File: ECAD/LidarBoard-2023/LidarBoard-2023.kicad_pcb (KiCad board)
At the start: 2 copper layers, 68.8 x 76.2 mm, 17 parts, among them J1 Serial_Strategy, J2 Serial_Lidar, J3 Conn_01x03, J4 Oled, U1 Teensy3.2, U2 AMS1117-3.3

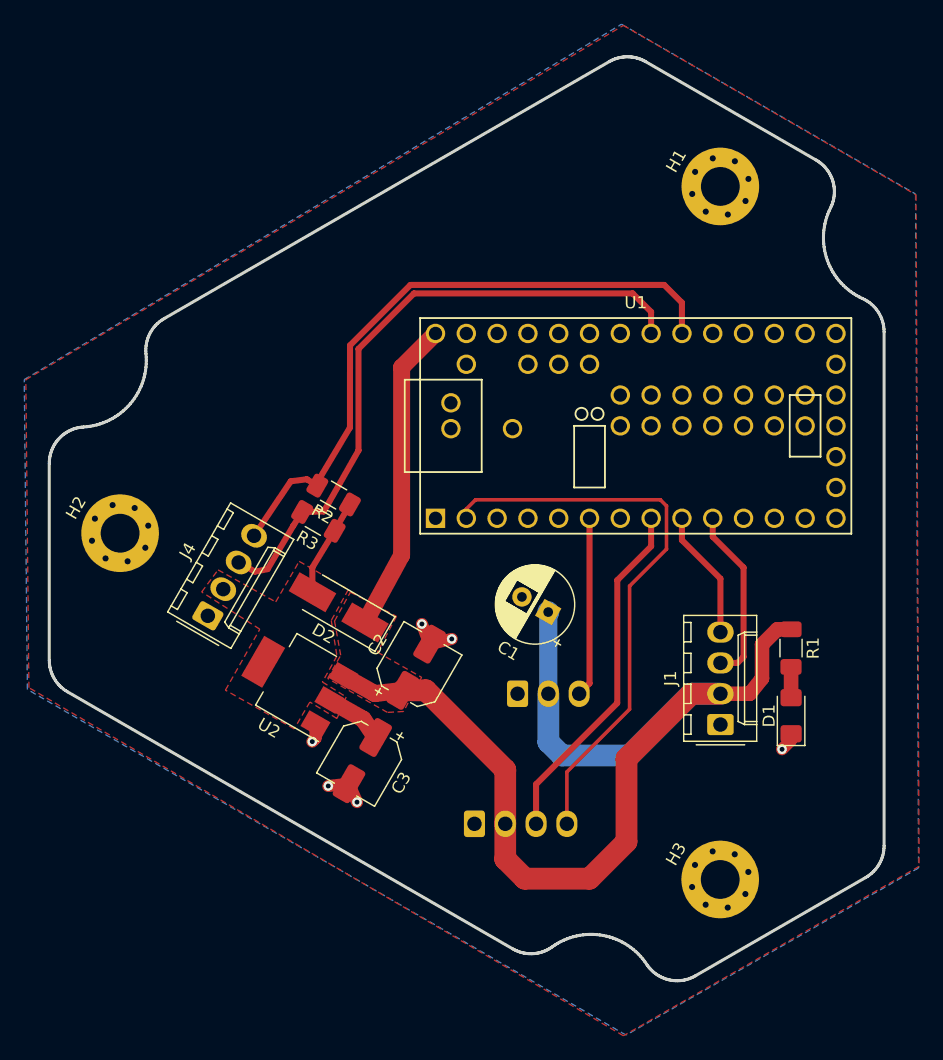
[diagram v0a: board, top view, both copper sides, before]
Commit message: Capacitor & silkscreen
Change output capacitor type to tantalum 1206 - 22uF
Update Silkscreen before production
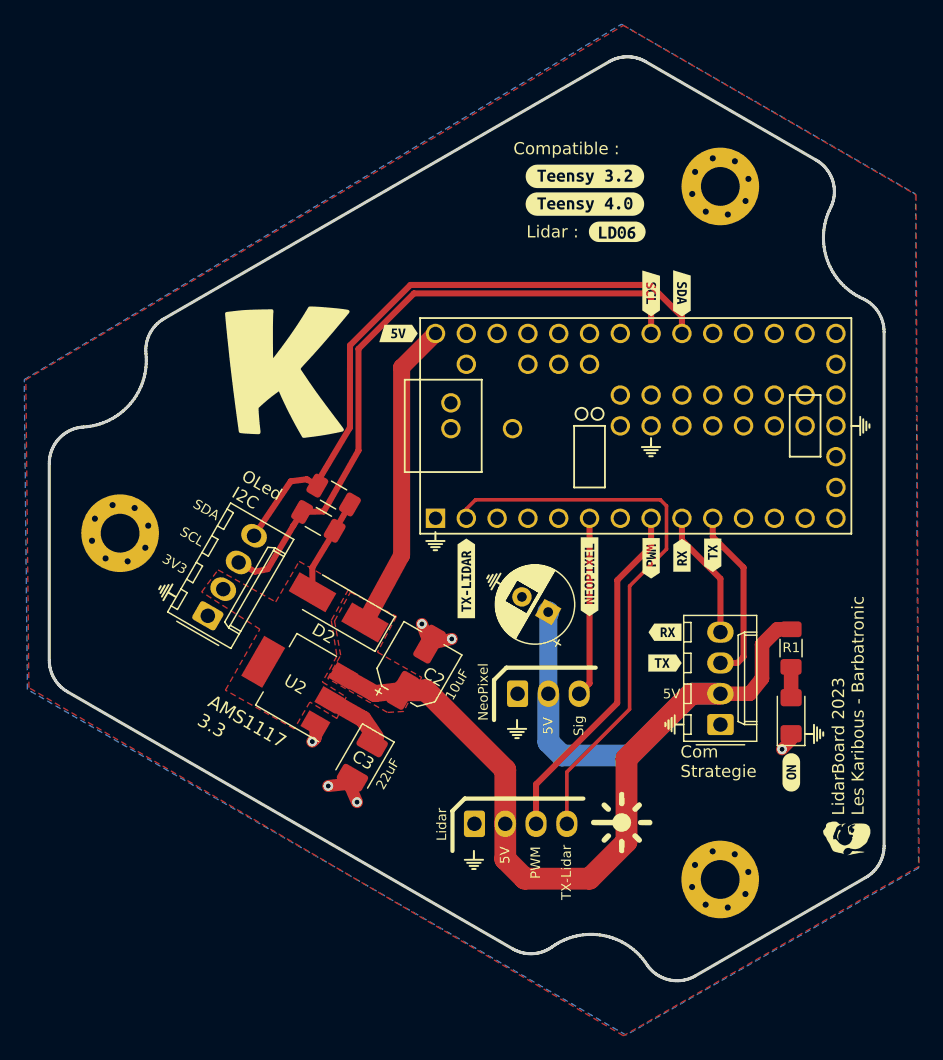
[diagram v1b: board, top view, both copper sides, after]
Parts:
- added G***: LOGO, LOGO, F.Cu at (157.5, 80.5)
- added G***: LOGO, LOGO, F.Cu at (174.8, 78.7)
- added G***: LOGO, LOGO, F.Cu at (170.9, 104.1)
- added G***: LOGO, LOGO, B.Cu at (142.9, 115.2)
- added G***: LOGO, LOGO, B.Cu at (146.4, 104.5)
- added G***: LOGO, LOGO, B.Cu at (159.3, 113.9)
- added G***: LOGO, LOGO, F.Cu at (117.6, 92.5)
- added G***: LOGO, LOGO, F.Cu at (146.4, 103.8)
- added G***: LOGO, LOGO, F.Cu at (159.3, 109.0)
- added G***: LOGO, LOGO, F.Cu at (139.7, 88.3)
- added G***: LOGO, LOGO, F.Cu at (142.9, 114.6)
- added G***: LOGO, LOGO, F.Cu at (144.7, 91.6)
- added G***: LOGO, LOGO, F.Cu at (159.4, 103.4)
- added G***: LOGO, LOGO, F.Cu at (173.6, 112.8)
- added kibuzzard-62EFEF5E: G***, kibuzzard-62EFEF5E, F.Cu at (152.0, 58.2)
- added kibuzzard-62EFEF6E: G***, kibuzzard-62EFEF6E, F.Cu at (152.0, 60.5)
- added kibuzzard-62EFEFDE: G***, kibuzzard-62EFEFDE, F.Cu at (154.7, 62.7)
- added kibuzzard-62EFF3FC: G***, kibuzzard-62EFF3FC, F.Cu at (160.0, 67.8)
- added kibuzzard-62EFF40D: G***, kibuzzard-62EFF40D, F.Cu at (157.5, 67.8)
- added kibuzzard-62EFF433: G***, kibuzzard-62EFF433, F.Cu at (136.7, 71.1)
- added kibuzzard-62EFF540: G***, kibuzzard-62EFF540, F.Cu at (169.0, 107.3)
- added kibuzzard-62EFF59A: G***, kibuzzard-62EFF59A, F.Cu at (157.5, 89.7)
- added kibuzzard-62EFF5A1: G***, kibuzzard-62EFF5A1, F.Cu at (142.2, 91.3)
- added kibuzzard-62EFF5AD: G***, kibuzzard-62EFF5AD, F.Cu at (152.4, 91.2)
- added kibuzzard-62EFF6AD: G***, kibuzzard-62EFF6AD, F.Cu at (160.0, 89.4)
- added kibuzzard-62EFF6BC: G***, kibuzzard-62EFF6BC, F.Cu at (162.6, 89.4)
- added kibuzzard-62EFF766: G***, kibuzzard-62EFF766, F.Cu at (158.6, 95.8)
- added kibuzzard-62EFF774: G***, kibuzzard-62EFF774, F.Cu at (158.6, 98.3)
- C3: value 10uF -> 22uF; footprint Capacitor_SMD:CP_Elec_5x5.4 -> Capacitor_Tantalum_SMD:CP_EIA-3528-12_Kemet-T_Pad1.50x2.35mm_HandSolder
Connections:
- net RX-Strat renamed TX
- net TX-Strat renamed RX
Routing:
- net SDA: track 51.7 -> 51.0 mm
- net SCL: track 52.5 -> 53.2 mm
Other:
- board text added: "10uF"
- board text added: "22uF"
- board text added: "3V3"
- board text added: "5V"
- board text added: "AMS1117 3.3"
- board text added: "Com Strategie"
- board text added: "Compatible :"
- board text added: "Lidar"
- board text added: "Lidar :"
- board text added: "LidarBoard 2023 Les Karibous - Barbatronic"
- board text added: "NeoPixel"
- board text added: "OLed I2C"
- board text added: "PWM"
- board text added: "SCL"
- board text added: "SDA"
- board text added: "Sig"
- board text added: "TX-Lidar"
